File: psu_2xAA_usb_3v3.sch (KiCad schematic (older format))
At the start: 9 parts, among them Q1 CJ2302, Q2 CJ2305, U3 HX9193-33GB

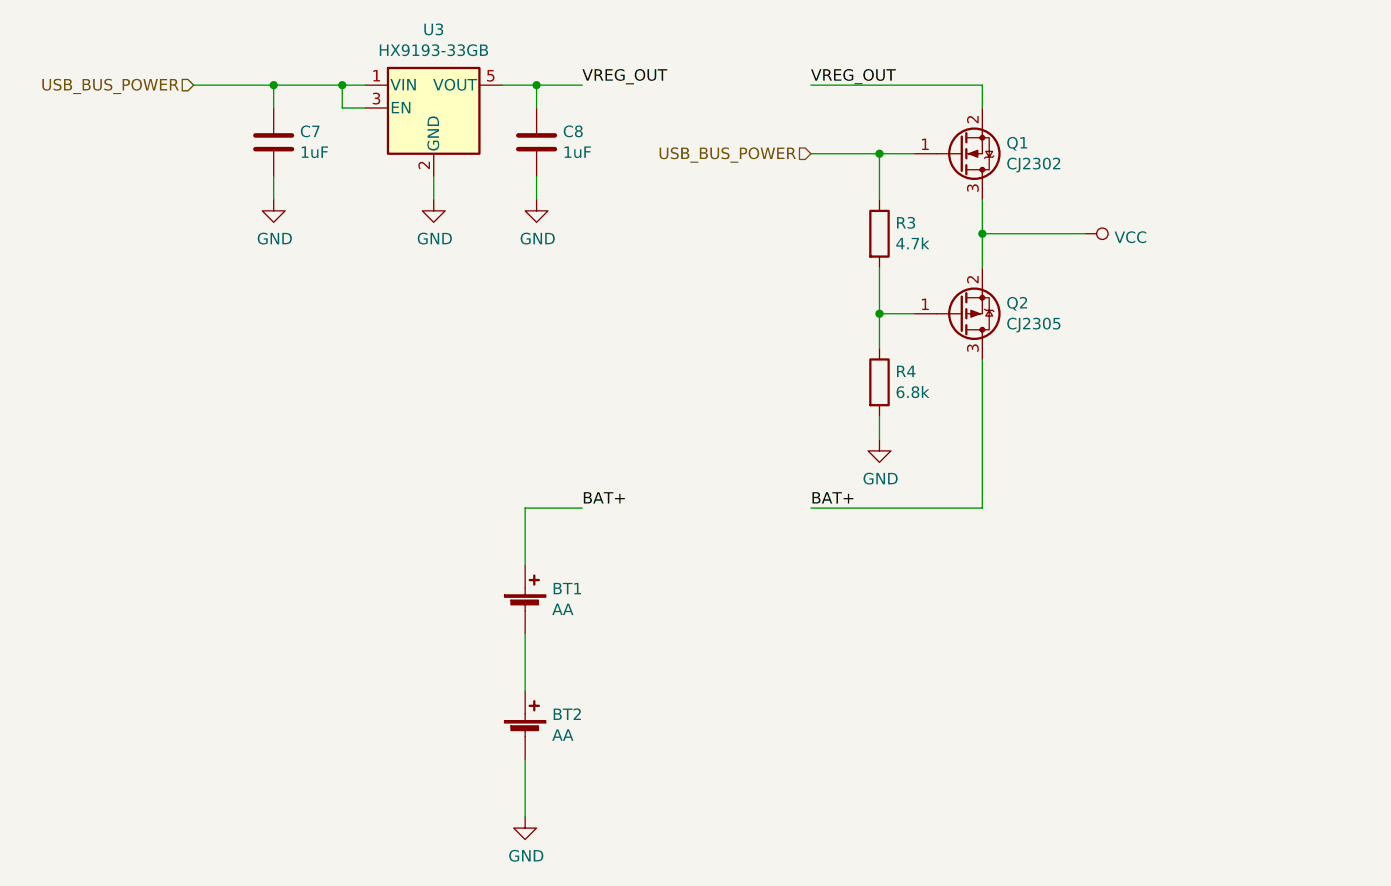
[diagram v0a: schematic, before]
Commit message: Updates to production version
Changed infrared setup, added step-up for battery power, added battery power switch, added more capacitors, changed and added logos, etc.
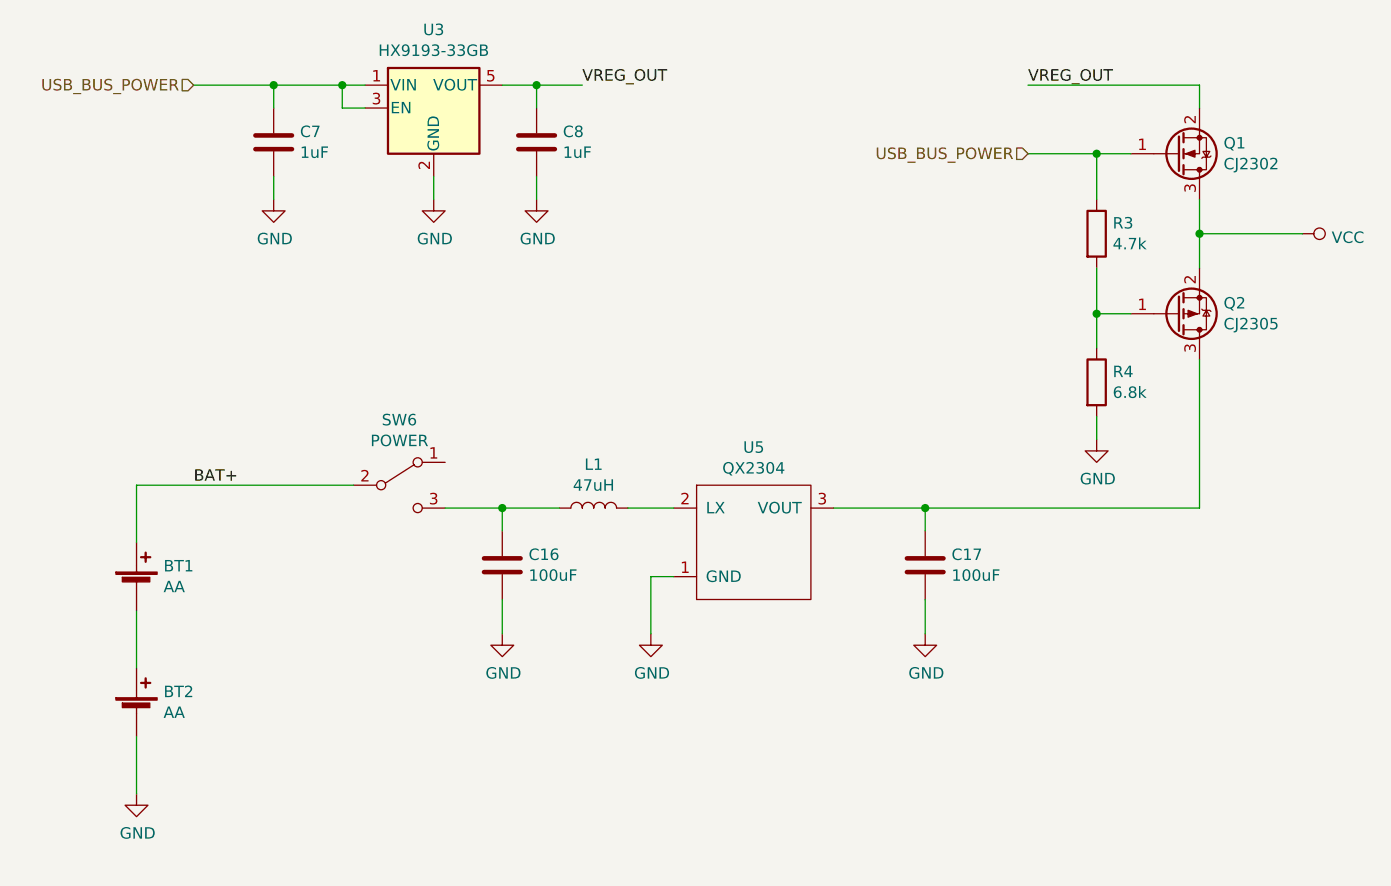
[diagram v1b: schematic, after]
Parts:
- added C16, C17: 100uF, Capacitors_SMD:C_1206, symbol device:C
- added L1: 47uH, Inductors_SMD:L_1210, symbol device:L
- added SW6: POWER, Buttons_Switches_SMD:SW_SPDT_PCM12, symbol Switch:SW_SPDT
- added U5: QX2304, TO_SOT_Packages_SMD:SOT-23, symbol Semiconductors:QX2304
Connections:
- net BAT+: now also SW6.2 (B); no longer Q2.3 (D)
- net GND: now also C16.2, C17.2, U5.1 (GND)
- new net: C17.1, Q2.3 (D), U5.3 (VOUT)
- new net: L1.2, U5.2 (LX)
- new net: C16.1, L1.1, SW6.3 (C)
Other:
- moved on the sheet: BT1, BT2, Q1, Q2, R3, R4
